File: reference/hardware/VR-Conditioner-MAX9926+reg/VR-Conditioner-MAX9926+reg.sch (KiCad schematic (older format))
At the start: 22 parts, among them J1 8-pin header, J2 Edge, U1 MAX9926UAEE+, U2 AMS1117CD-5.0

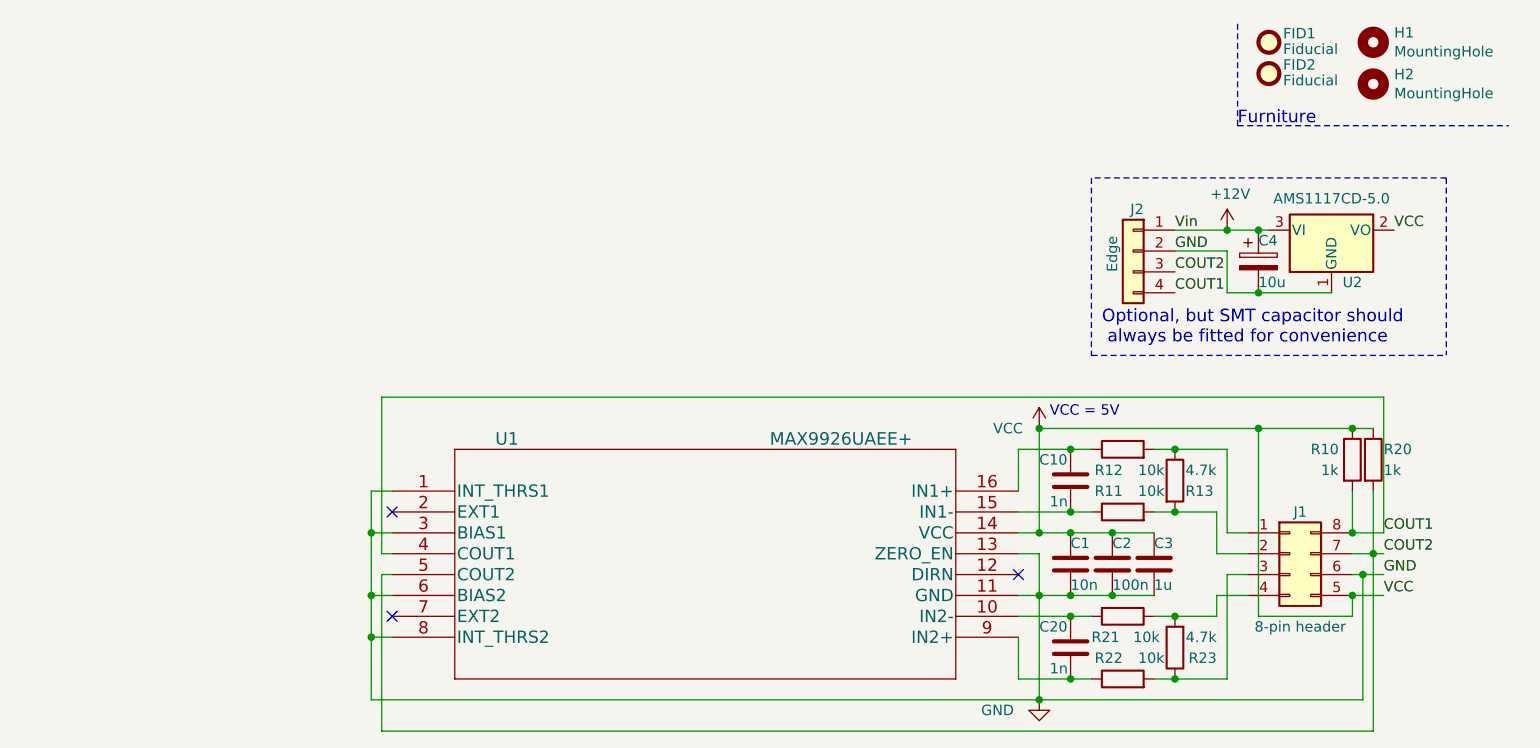
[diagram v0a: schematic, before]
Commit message: Reroute a trace to avoid 2 traces between a pair of pins.
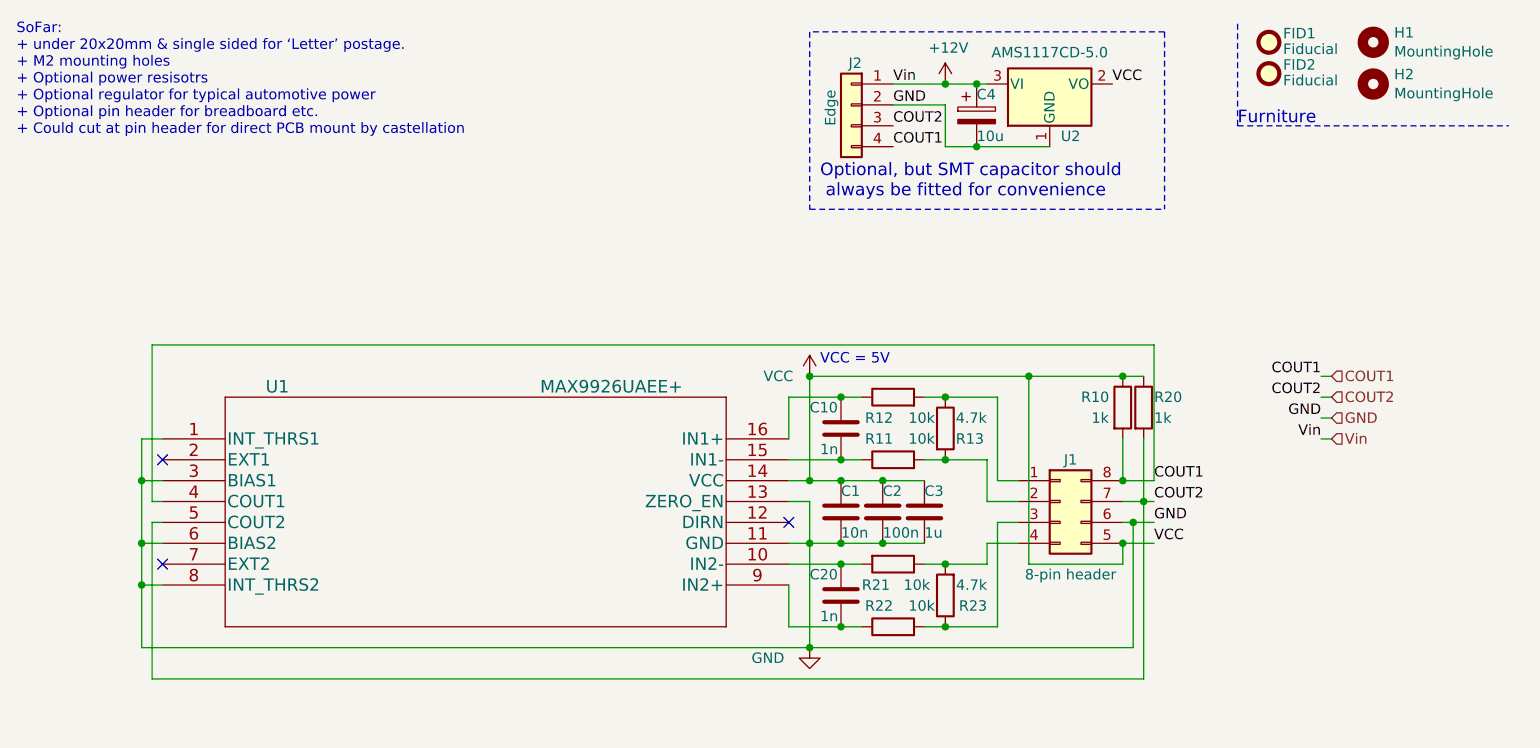
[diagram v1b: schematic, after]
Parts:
- C1: Description 50 V ±10 % Tolerance X7R Surface Mount Multilayer Ceramic -> 10 V ±5% Tolerance U2J Multilayer Ceramic Capacitor; MFG Name Kemet -> Murata Murata; MFG Part Num C0603X103G5JACTU -> GRM1857U1A103JA44D
- C10, C20: Description 100V ±10 % Tolerance X7R Surface Mount Multilayer Ceramic -> 1000 pF 50 V ±5 % Tolerance C0G SMT Multilayer Ceramic Capa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; MFG Name Kemet -> Murata; MFG Part Num C0603C102G5GACTU -> GRM1885C1H102JA01D
- C2: Description 50 V ±10 % Tolerance X7R Surface Mount Multilayer Ceramic -> Ceramic 0.1uF 16V X7R 10% Pad SMD 0603 Soft Termination 125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; MFG Name Multicomp -> Murata; MFG Part Num MC0603F104Z250CT -> GCJ188R71C104KA01D
- C3: Description 50 V ±10 % Tolerance X7R Surface Mount Multilayer Ceramic -> 16V ±10% Tolerance X7R Surface Mount Multilayer Ceramic Cap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; MFG Name Kemet -> Murata; MFG Part Num C0603C105Z3VACTU -> GCM188R71C105KA64D
- C4: Description Multilayer Ceramic Capacitors (High dielectric type), 25V, 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 -> 25 V 10 uF ±20% Tolerance X5R Multilayer Ceramic Capacitor; MFG Name Kemet -> Murata; MFG Part Num C0805C106K9PACTU -> GRM21BR61E106MA73L
- J2, R13, R23, U2: Critical No. Option for user install -> DoNoPlace. User option
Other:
- note added: "SoFar:\n+ under 20x20mm & single sided for ‘Letter’ postage.\n+ M2 mounting holes\n+ Optional power resisotrs\n+ Optional regulator for typical automotive power\n+ Optional pin header for breadboard etc. \n+ Could cut at pin header for direct PCB mount by castellation"
- moved on the sheet: C1, C10, C2, C20, C3, C4, J1, J2, R10, R11, R12, R13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
